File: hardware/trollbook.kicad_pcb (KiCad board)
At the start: 2 copper layers, 100 x 100 mm, 97 parts, among them P1 VGA, P10 CONN_1, P11 CONN_2, P2 LCD_CONN, P3 SPI, P4 CONN_12, P5 CONN_2, P6 CONN_2, P7 CONN_2, P8 CONN_4, P9 CONN_2, U1 XC95288-208, U10 74LVC574, U11 74LVC574, U12 HY57V561620, U13 HY57V561620, U15 74HC4002, U16 ADA4851-4, U19 74HC139, U2 MC68030, U20 74LVC10, U3 MC68882, U4 IDT71V416, U5 TLC7524, U6 74LVC574, U7 39F040, U8 TLC7524, U9 74LVC574, Y1 50 MHz, Y2 12.288 MHz

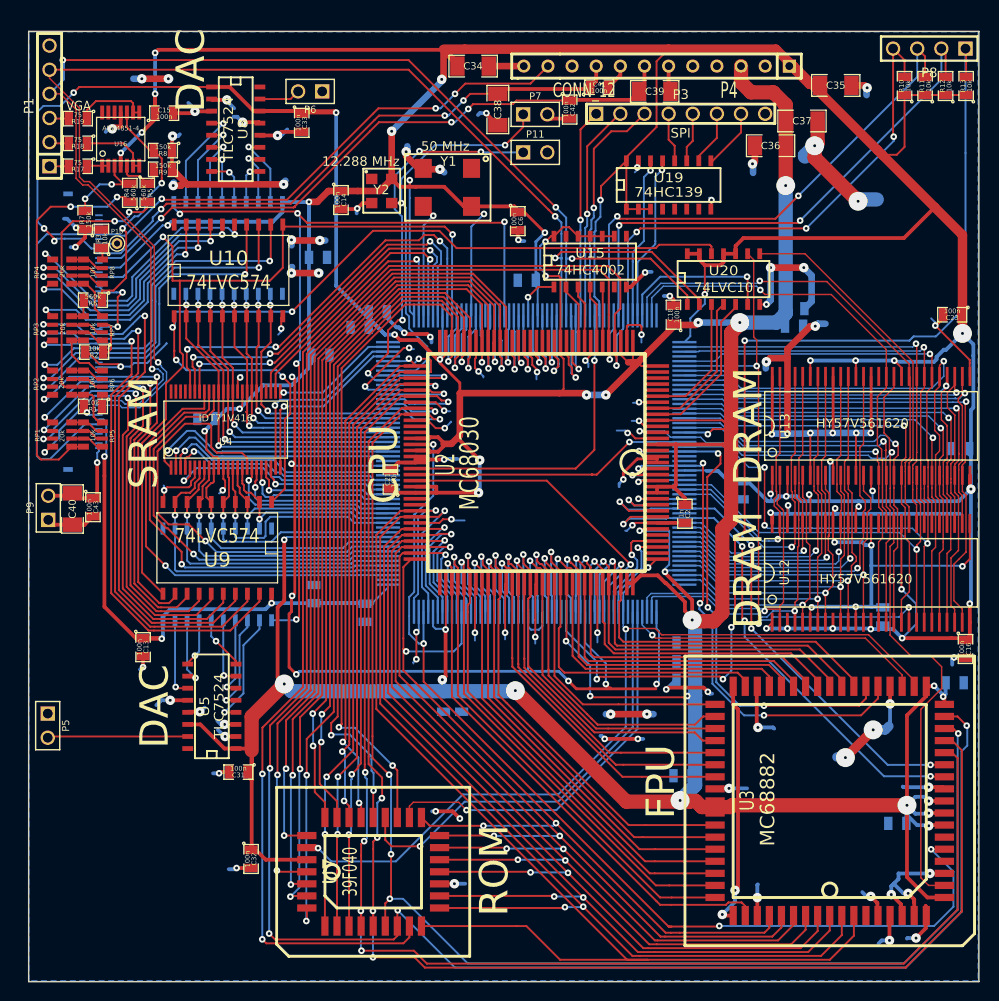
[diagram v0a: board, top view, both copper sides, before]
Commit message: replaced ram footprint with the correct one
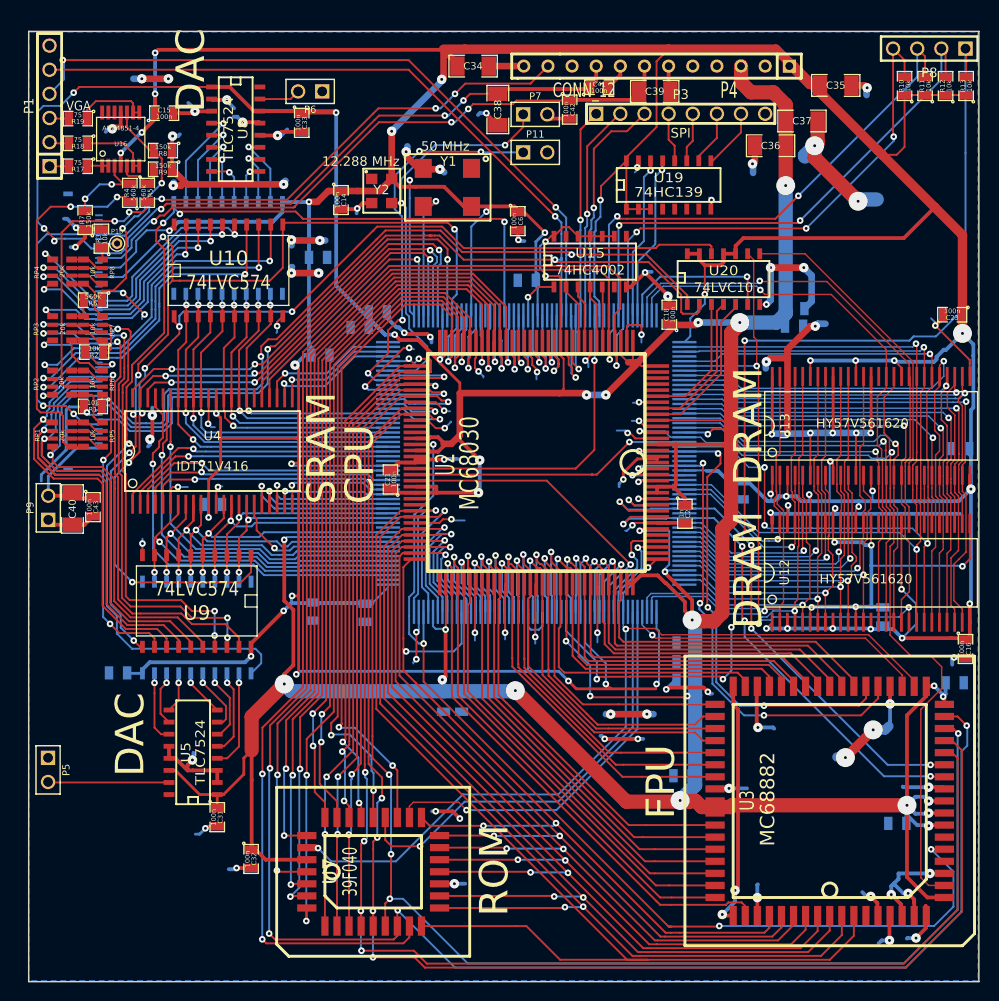
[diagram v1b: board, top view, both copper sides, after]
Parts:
- C13: moved to B.Cu
- U4: footprint TSSOP-48 -> TSOP44
- moved C24 28.3 mm to (98.9, 208.5)
- moved C13 16.7 mm to (108.9, 190.8), turned to 0 degrees
- moved U6 5.99 mm to (107.2, 203.7)
- moved U9 5.99 mm to (107.2, 200.9)
- moved C31 5.24 mm to (109.3, 223.7), turned to 270 degrees
- moved U5 5.22 mm to (106.8, 216.9)
- moved P5 4.66 mm to (91.5, 218.7)
- moved U4 2.66 mm to (108.8, 185.2)
- moved C26 1.85 mm to (119.4, 202.1), turned to 270 degrees
- moved C18 0.43 mm to (156.9, 170.8)
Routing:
- net /LLWEN: track 47.2 -> 17.7 mm
- net /SNDLATCH: track 92.0 -> 114.3 mm, vias 5 -> 4
- net /VGAHSYNC: track 134.0 -> 154.1 mm
- net /VGAVSYNC: track 135.6 -> 152.8 mm
- net /VGAOE: track 94.7 -> 109.7 mm, vias 4 -> 6
- net /VGAB2: track 44.1 -> 54.2 mm, vias 2 -> 1
- net /VGALATCH: track 92.9 -> 101.0 mm, vias 2 -> 6
- net /LLA11: track 20.8 -> 13.3 mm
- net /VGAB3: track 45.3 -> 52.7 mm, vias 2 -> 1
- net 3V3: track 706.0 -> 712.5 mm, vias 43 -> 42
- net /VCOM: track 92.2 -> 86.3 mm, vias 3 -> 5
- net /LLBLE: track 43.7 -> 37.9 mm
- net /LLA12: track 19.7 -> 13.9 mm
- net /LLBHE: track 45.4 -> 40.0 mm
- net /VGAG2: track 57.2 -> 51.9 mm
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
